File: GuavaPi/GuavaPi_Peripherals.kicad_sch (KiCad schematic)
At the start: 1 part

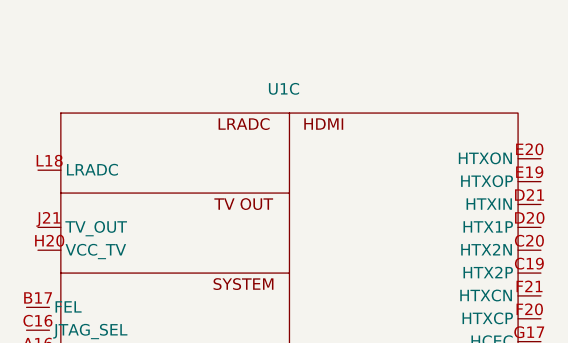
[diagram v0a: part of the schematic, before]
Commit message: Started DRAM Design
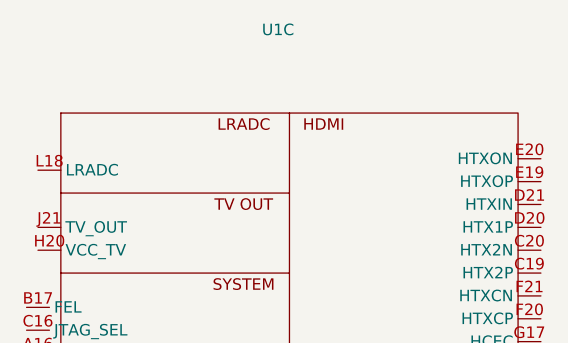
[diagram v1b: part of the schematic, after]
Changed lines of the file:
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@@
   (symbol (lib_id "Allwinner_H616:Allwinner_H616") (at 32.6136 28.9052 0) (unit 3)
     (in_bom yes) (on_board yes) (dnp no) (fields_autoplaced)
-    (property "Reference" "U1" (at 70.0786 37.6936 0)
+    (property "Reference" "U1" (at 69.4436 31.0896 0)
       (effects (font (size 1.27 1.27)))
     )
@@
           (reference "U1") (unit 3)
         )
+        (path "/3be7235b-2d12-456d-bbdb-dcc9c2ae1afd/dc1a4d83-a933-4336-ba01-88286996a5dc"
+          (reference "U1") (unit 3)
+        )

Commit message: Misc
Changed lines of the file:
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@@
     (pin "C20")
     (pin "D11")
+    (pin "D12")
     (pin "D13")
     (pin "D14")
@@
     (pin "B6")
     (pin "D10")
-    (pin "D12")
     (pin "D19")
-    (pin "F10")
     (pin "F10")
     (pin "F11")
@@
     (pin "F8")
     (pin "F9")
-    (pin "F9")
     (pin "G10")
     (pin "G11")
@@
     (pin "G15")
     (pin "G8")
-    (pin "G8")
-    (pin "G9")
     (pin "G9")
     (pin "H10")
@@
     (pin "K9")
     (pin "L21")
-    (pin "L8")
     (pin "L8")
     (pin "M1")
@@
           (reference "U1") (unit 3)
         )
+        (path "/3be7235b-2d12-456d-bbdb-dcc9c2ae1afd/0e09d813-5fde-42ce-9948-43290a465bd7"
+          (reference "U1") (unit 3)
+        )

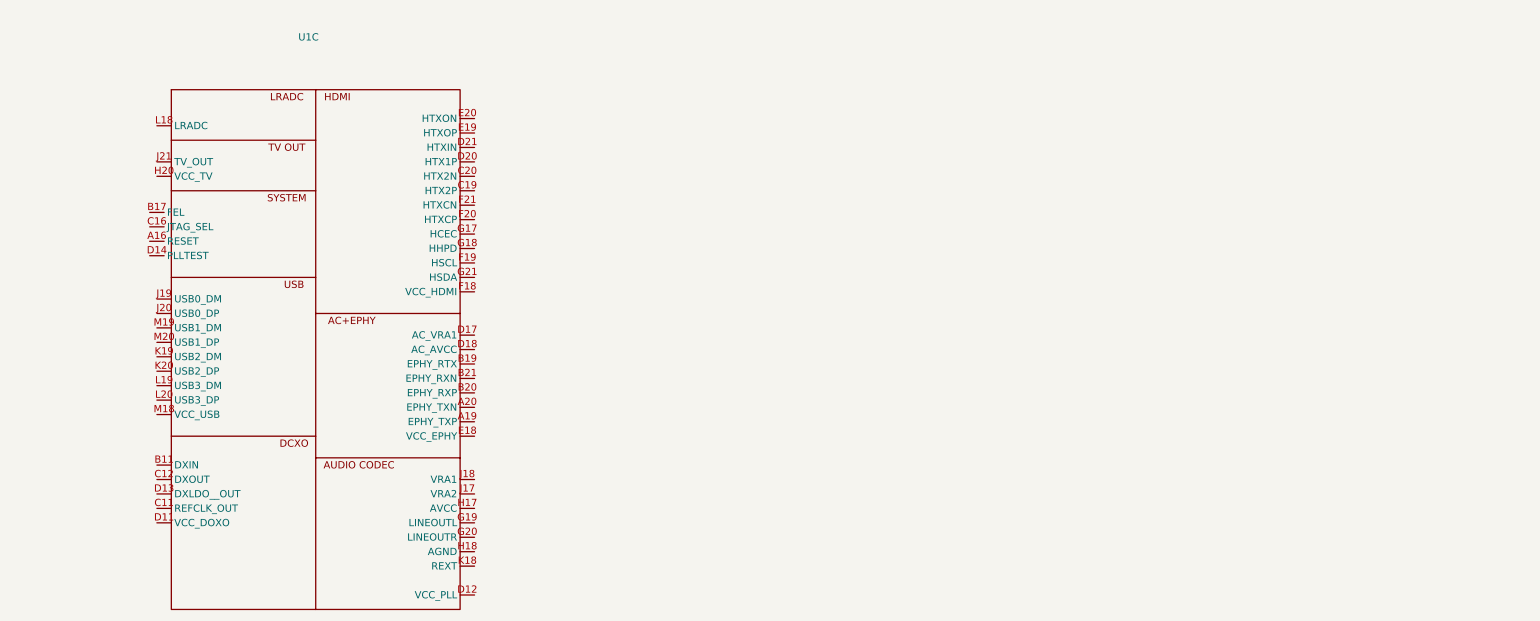
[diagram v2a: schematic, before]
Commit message: Added USB-C
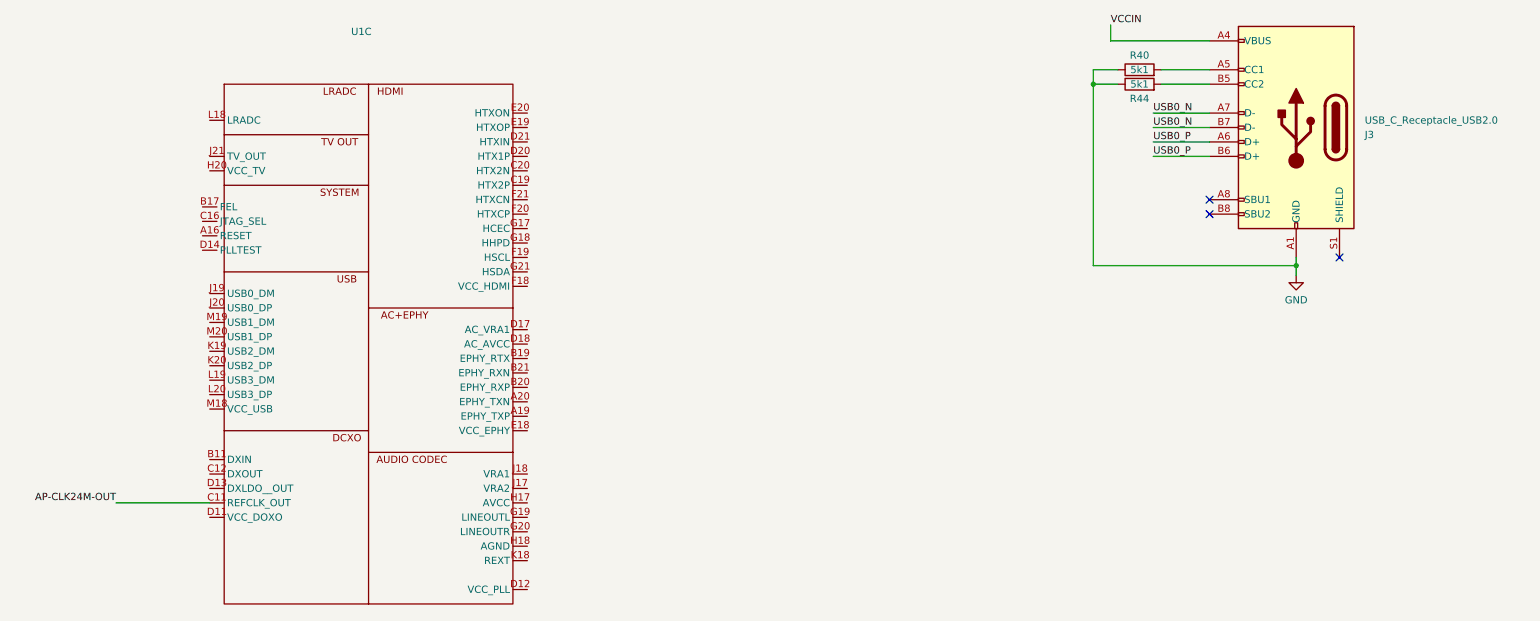
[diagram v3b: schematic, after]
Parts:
- added J3: USB_C_Receptacle_USB2.0, symbol Connector:USB_C_Receptacle_USB2.0
- added R40, R44: 5k1, symbol Device:R
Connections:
- net AP-CLK24M-OUT: now reaches U1.C11 (REFCLK_OUT)
- new net: J3.A5 (CC1), R40.2
- new net: J3.B5 (CC2), R44.2
- new net GND: J3.A1 (GND), J3.A12 (GND), J3.B1 (GND), J3.B12 (GND), R40.1, R44.1
- new net USB0_N: J3.A7 (D-), J3.B7 (D-)
- new net USB0_P: J3.A6 (D+), J3.B6 (D+)
- new net VCCIN: J3.A4 (VBUS), J3.A9 (VBUS), J3.B4 (VBUS), J3.B9 (VBUS)
- no-connect marks 0 -> 3
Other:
- moved on the sheet: U1C
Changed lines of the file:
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@@
 (kicad_sch (version 20230121) (generator eeschema)
   (paper "A4")
-  (symbol (lib_id "Allwinner_H616:Allwinner_H616") (at 32.6136 28.9052 0) (unit 3)
+  (junction (at 243.205 71.284) (diameter 0) (color 0 0 0 0)
+  )
+  (junction (at 207.518 39.37) (diameter 0) (color 0 0 0 0)
+  )
+  (no_connect (at 250.825 69.85))
+  (no_connect (at 227.965 62.23))
+  (no_connect (at 227.965 59.69))
+  (wire (pts (xy 227.965 39.37) (xy 219.456 39.37))
+    (stroke (width 0) (type default))
+  )
+  (wire (pts (xy 210.566 28.956) (xy 210.566 31.75))
+    (stroke (width 0) (type default))
+  )
+  (wire (pts (xy 219.456 36.83) (xy 227.965 36.83))
+    (stroke (width 0) (type default))
+  )
+  (wire (pts (xy 243.205 69.85) (xy 243.205 71.284))
+    (stroke (width 0) (type default))
+  )
+  (wire (pts (xy 227.965 31.75) (xy 210.566 31.75))
+    (stroke (width 0) (type default))
+  )
+  (wire (pts (xy 227.965 46.99) (xy 218.059 46.99))
+    (stroke (width 0) (type default))
+  )
+  (wire (pts (xy 227.965 49.53) (xy 218.059 49.53))
+    (stroke (width 0) (type default))
+  )
+  (wire (pts (xy 218.059 44.45) (xy 227.965 44.45))
+    (stroke (width 0) (type default))
+  )
+  (wire (pts (xy 207.518 71.284) (xy 243.205 71.284))
+    (stroke (width 0) (type default))
+  )
+  (wire (pts (xy 35.5854 113.03) (xy 52.07 113.03))
+    (stroke (width 0) (type default))
+  )
+  (wire (pts (xy 207.518 39.37) (xy 207.518 71.284))
+    (stroke (width 0) (type default))
+  )
+  (wire (pts (xy 207.518 36.83) (xy 207.518 39.37))
+    (stroke (width 0) (type default))
+  )
+  (wire (pts (xy 227.965 52.07) (xy 218.059 52.07))
+    (stroke (width 0) (type default))
+  )
+  (wire (pts (xy 211.836 39.37) (xy 207.518 39.37))
+    (stroke (width 0) (type default))
+  )
+  (wire (pts (xy 211.836 36.83) (xy 207.518 36.83))
+    (stroke (width 0) (type default))
+  )
+  (wire (pts (xy 243.205 71.284) (xy 243.205 73.025))
+    (stroke (width 0) (type default))
+  )
+  (label "USB0_P" (at 218.059 52.07 0) (fields_autoplaced)
+    (effects (font (size 1.27 1.27)) (justify left bottom))
+  )
+  (label "VCCIN" (at 210.566 28.956 0) (fields_autoplaced)
+    (effects (font (size 1.27 1.27)) (justify left bottom))
+  )
+  (label "USB0_N" (at 218.059 46.99 0) (fields_autoplaced)
+    (effects (font (size 1.27 1.27)) (justify left bottom))
+  )
+  (label "AP-CLK24M-OUT" (at 35.5854 113.03 180) (fields_autoplaced)
+    (effects (font (size 1.27 1.27)) (justify right bottom))
+  )
+  (label "USB0_N" (at 218.059 44.45 0) (fields_autoplaced)
+    (effects (font (size 1.27 1.27)) (justify left bottom))
+  )
+  (label "USB0_P" (at 218.059 49.53 0) (fields_autoplaced)
+    (effects (font (size 1.27 1.27)) (justify left bottom))
+  )
+  (symbol (lib_id "power:GND") (at 243.205 73.025 0) (mirror y) (unit 1)
     (in_bom yes) (on_board yes) (dnp no) (fields_autoplaced)
-    (property "Reference" "U1" (at 69.4436 31.0896 0)
-      (effects (font (size 1.27 1.27)))
-    )
-    (property "Value" "~" (at 32.6136 28.9052 0)
-      (effects (font (size 1.27 1.27)))
-    )
-    (property "Footprint" "" (at 32.6136 28.9052 0)
-      (effects (font (size 1.27 1.27)) hide)
-    )
-    (property "Datasheet" "" (at 32.6136 28.9052 0)
+    (property "Reference" "#PWR030" (at 243.205 79.375 0)
+      (effects (font (size 1.27 1.27)) hide)
+    )
+    (property "Value" "GND" (at 243.205 77.346 0)
+      (effects (font (size 1.27 1.27)))
+    )
+    (property "Footprint" "" (at 243.205 73.025 0)
+      (effects (font (size 1.27 1.27)) hide)
+    )
+    (property "Datasheet" "" (at 243.205 73.025 0)
+      (effects (font (size 1.27 1.27)) hide)
+    )
+    (pin "1")
+    (instances
+      (project "GuavaPi"
+        (path "/3be7235b-2d12-456d-bbdb-dcc9c2ae1afd/cdc4c29d-b8ce-4a88-b280-649e912d2091"
+          (reference "#PWR030") (unit 1)
+        )
+      )
+    )
+  )
+  (symbol (lib_id "Device:R") (at 215.646 36.83 90) (unit 1)
+    (in_bom yes) (on_board yes) (dnp no)
+    (property "Reference" "R40" (at 215.646 34.29 90)
+      (effects (font (size 1.27 1.27)))
+    )
+    (property "Value" "5k1" (at 215.646 36.83 90)
+      (effects (font (size 1.27 1.27)))
+    )
+    (property "Footprint" "" (at 215.646 38.608 90)
+      (effects (font (size 1.27 1.27)) hide)
+    )
+    (property "Datasheet" "~" (at 215.646 36.83 0)
+      (effects (font (size 1.27 1.27)) hide)
+    )
+    (pin "1")
+    (pin "2")
+    (instances
+      (project "GuavaPi"
+        (path "/3be7235b-2d12-456d-bbdb-dcc9c2ae1afd/cdc4c29d-b8ce-4a88-b280-649e912d2091"
+          (reference "R40") (unit 1)
+        )
+      )
+    )
+  )
+  (symbol (lib_id "Connector:USB_C_Receptacle_USB2.0") (at 243.205 46.99 0) (mirror y) (unit 1)
+    (in_bom yes) (on_board yes) (dnp no) (fields_autoplaced)
+    (property "Reference" "J3" (at 255.27 48.26 0)
+      (effects (font (size 1.27 1.27)) (justify right))
+    )
+    (property "Value" "USB_C_Receptacle_USB2.0" (at 255.27 45.72 0)
+      (effects (font (size 1.27 1.27)) (justify right))
+    )
+    (property "Footprint" "" (at 239.395 46.99 0)
+      (effects (font (size 1.27 1.27)) hide)
+    )
+    (property "Datasheet" "https://www.usb.org/sites/default/files/documents/usb_type-c.zip" (at 239.395 46.99 0)
+      (effects (font (size 1.27 1.27)) hide)
+    )
+    (pin "A1")
+    (pin "A12")
+    (pin "A4")
+    (pin "A5")
+    (pin "A6")
+    (pin "A7")
+    (pin "A8")
+    (pin "A9")
+    (pin "B1")
+    (pin "B12")
+    (pin "B4")
+    (pin "B5")
+    (pin "B6")
+    (pin "B7")
+    (pin "B8")
+    (pin "B9")
+    (pin "S1")
+    (instances
+      (project "GuavaPi"
+        (path "/3be7235b-2d12-456d-bbdb-dcc9c2ae1afd/cdc4c29d-b8ce-4a88-b280-649e912d2091"
+          (reference "J3") (unit 1)
+        )
+      )
+    )
+  )
+  (symbol (lib_id "Device:R") (at 215.646 39.37 90) (unit 1)
+    (in_bom yes) (on_board yes) (dnp no)
+    (property "Reference" "R44" (at 215.646 41.91 90)
+      (effects (font (size 1.27 1.27)))
+    )
+    (property "Value" "5k1" (at 215.646 39.37 90)
+      (effects (font (size 1.27 1.27)))
+    )
+    (property "Footprint" "" (at 215.646 41.148 90)
+      (effects (font (size 1.27 1.27)) hide)
+    )
+    (property "Datasheet" "~" (at 215.646 39.37 0)
+      (effects (font (size 1.27 1.27)) hide)
+    )
+    (pin "1")
+    (pin "2")
+    (instances
+      (project "GuavaPi"
+        (path "/3be7235b-2d12-456d-bbdb-dcc9c2ae1afd/cdc4c29d-b8ce-4a88-b280-649e912d2091"
+          (reference "R44") (unit 1)
+        )
+      )
+    )
+  )
+  (symbol (lib_id "Allwinner_H616:Allwinner_H616") (at 41.91 27.94 0) (unit 3)
+    (in_bom yes) (on_board yes) (dnp no) (fields_autoplaced)
+    (property "Reference" "U1" (at 78.74 30.1244 0)
+      (effects (font (size 1.27 1.27)))
+    )
+    (property "Value" "~" (at 41.91 27.94 0)
+      (effects (font (size 1.27 1.27)))
+    )
+    (property "Footprint" "" (at 41.91 27.94 0)
+      (effects (font (size 1.27 1.27)) hide)
+    )
+    (property "Datasheet" "" (at 41.91 27.94 0)
       (effects (font (size 1.27 1.27)) hide)
     )
@@
           (reference "U1") (unit 3)
         )
+        (path "/3be7235b-2d12-456d-bbdb-dcc9c2ae1afd/ee47a8ed-1560-4850-b72b-05512224a0ba"
+          (reference "U1") (unit 3)
+        )
